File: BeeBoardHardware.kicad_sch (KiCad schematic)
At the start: 34 parts, among them J2 USB_C_Receptacle_USB2.0_16P, J3 Conn_01x02, Q1 Q_PMOS_DGS, Q2 2N3904, SW1 SW_Push, U1 MCP16311x-xMNY, U2 BQ24074RGT, U3 USBLC6-2SC6

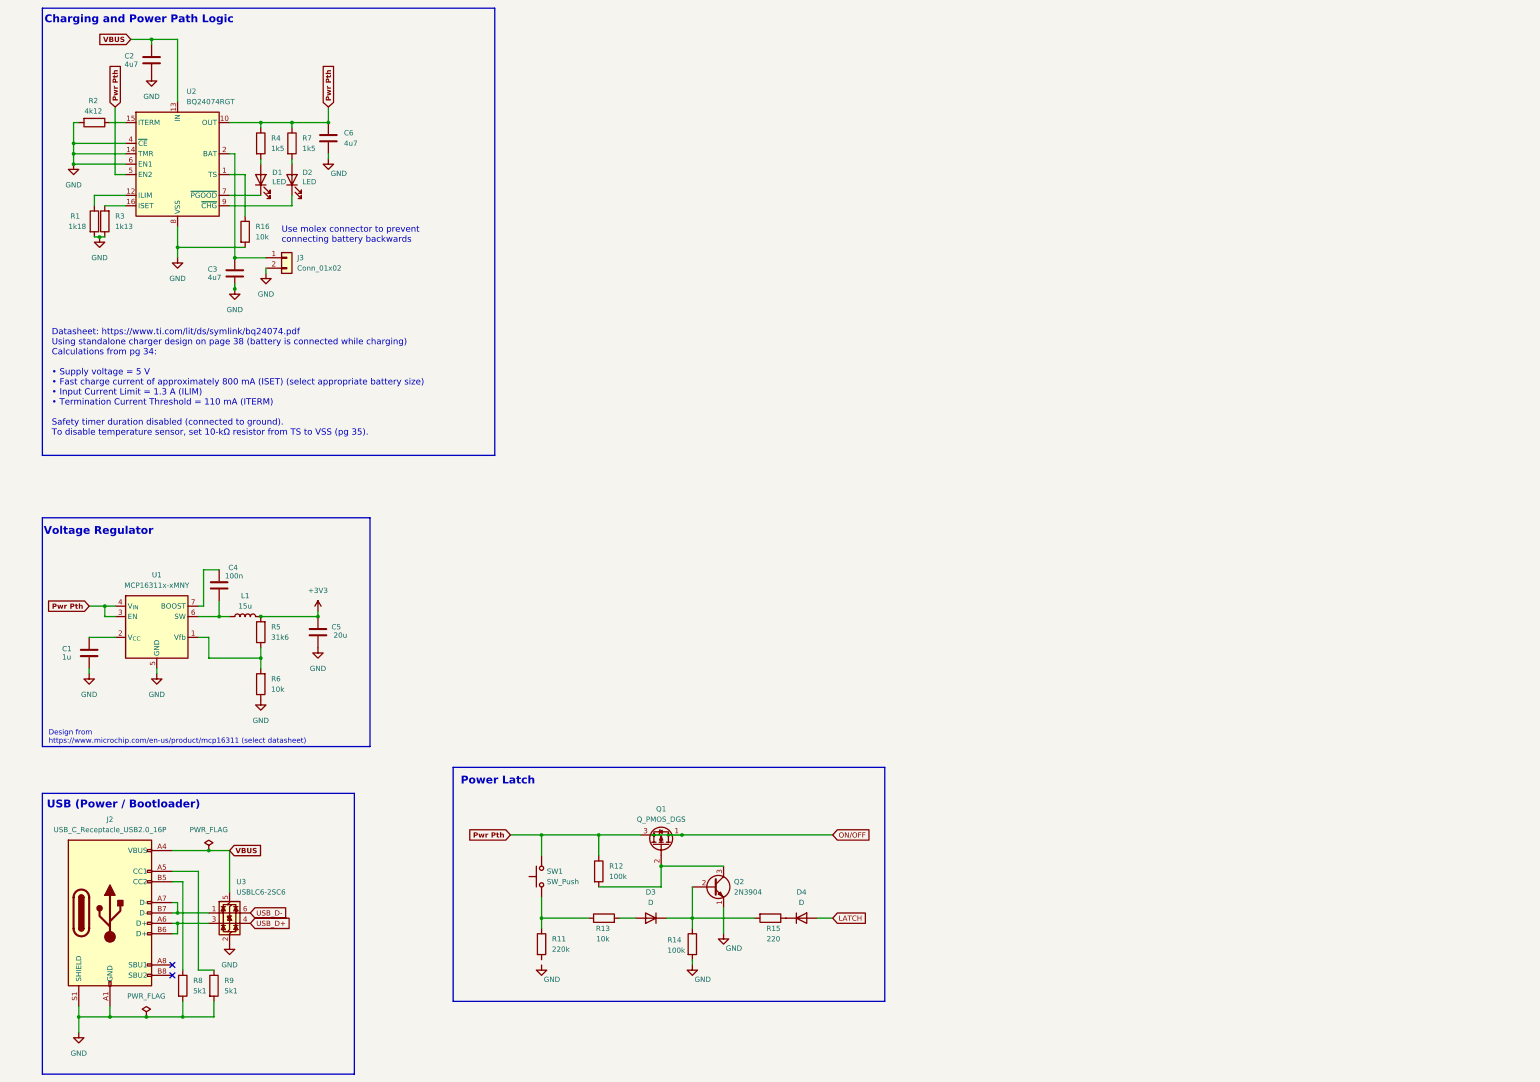
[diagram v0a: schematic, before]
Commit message: add readme and updated schematic
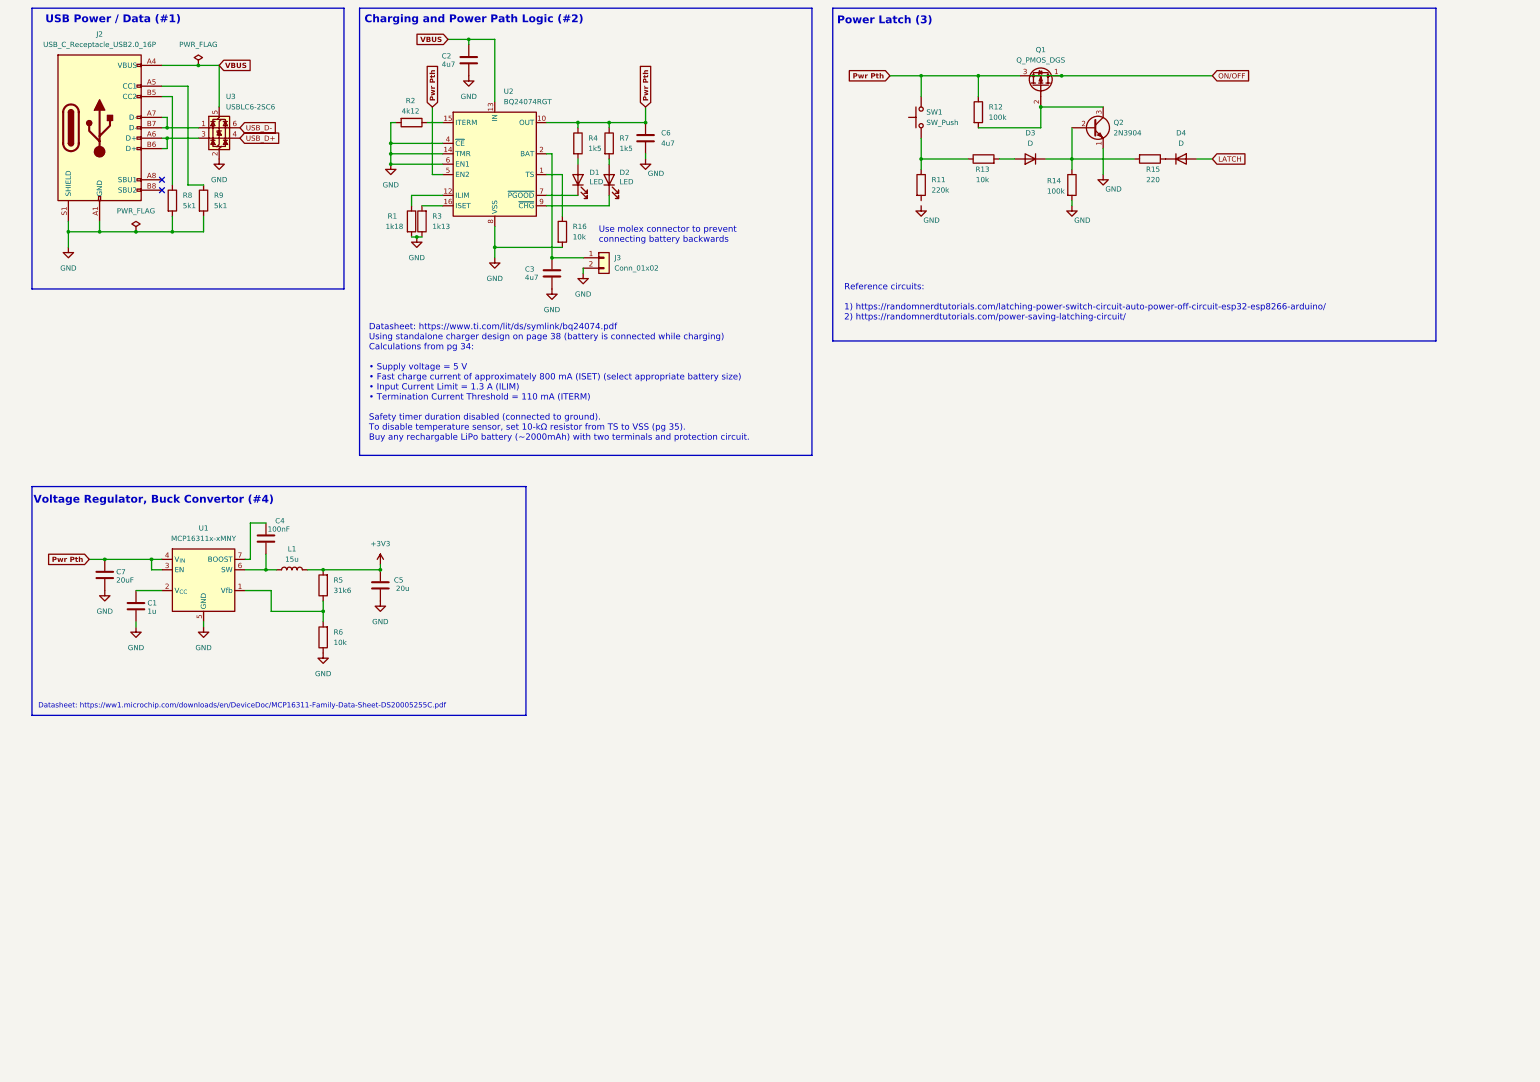
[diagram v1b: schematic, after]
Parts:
- added C7: 20uF, Capacitor_SMD:C_0402_1005Metric, symbol Device:C
- C4: value 100n -> 100nF
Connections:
- net GND: now also C7.2
- net Pwr Pth: now also C7.1
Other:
- note added: "Charging and Power Path Logic (#2)"
- note added: "Datasheet: https://ww1.microchip.com/downloads/en/DeviceDoc/MCP16311-Family-Data-Sheet-DS20005255C.pdf"
- note added: "Power Latch (3)"
- note added: "Reference circuits: 1) https://randomnerdtutorials.com/latching-power-switch-circuit-auto-power-off-circuit-esp32-esp8266-arduino/ 2) https://randomnerdtutorials.com/power-saving-latching-circuit/"
- note added: "USB Power / Data (#1)"
- note added: "Voltage Regulator, Buck Convertor (#4)"
- note removed: "Charging and Power Path Logic"
- note removed: "Design from https://www.microchip.com/en-us/product/mcp16311 (select datasheet)"
- note removed: "Power Latch"
- note removed: "USB (Power / Bootloader)"
- note removed: "Voltage Regulator"
- moved on the sheet: C1, C2, C3, C4, C5, C6, D1, D2, D3, D4, J2, J3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

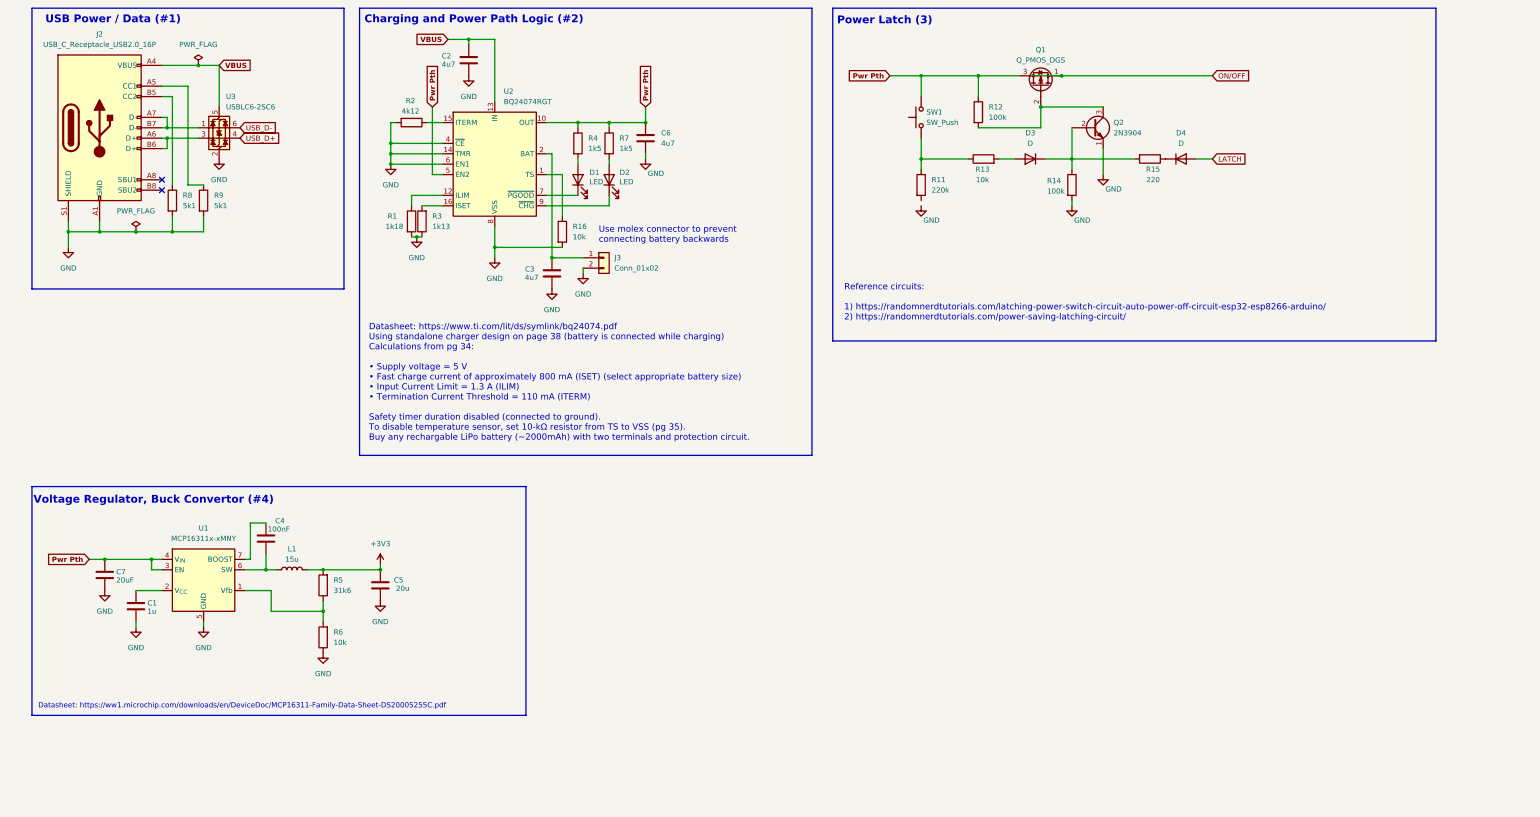
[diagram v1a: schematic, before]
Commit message: added battery monitor
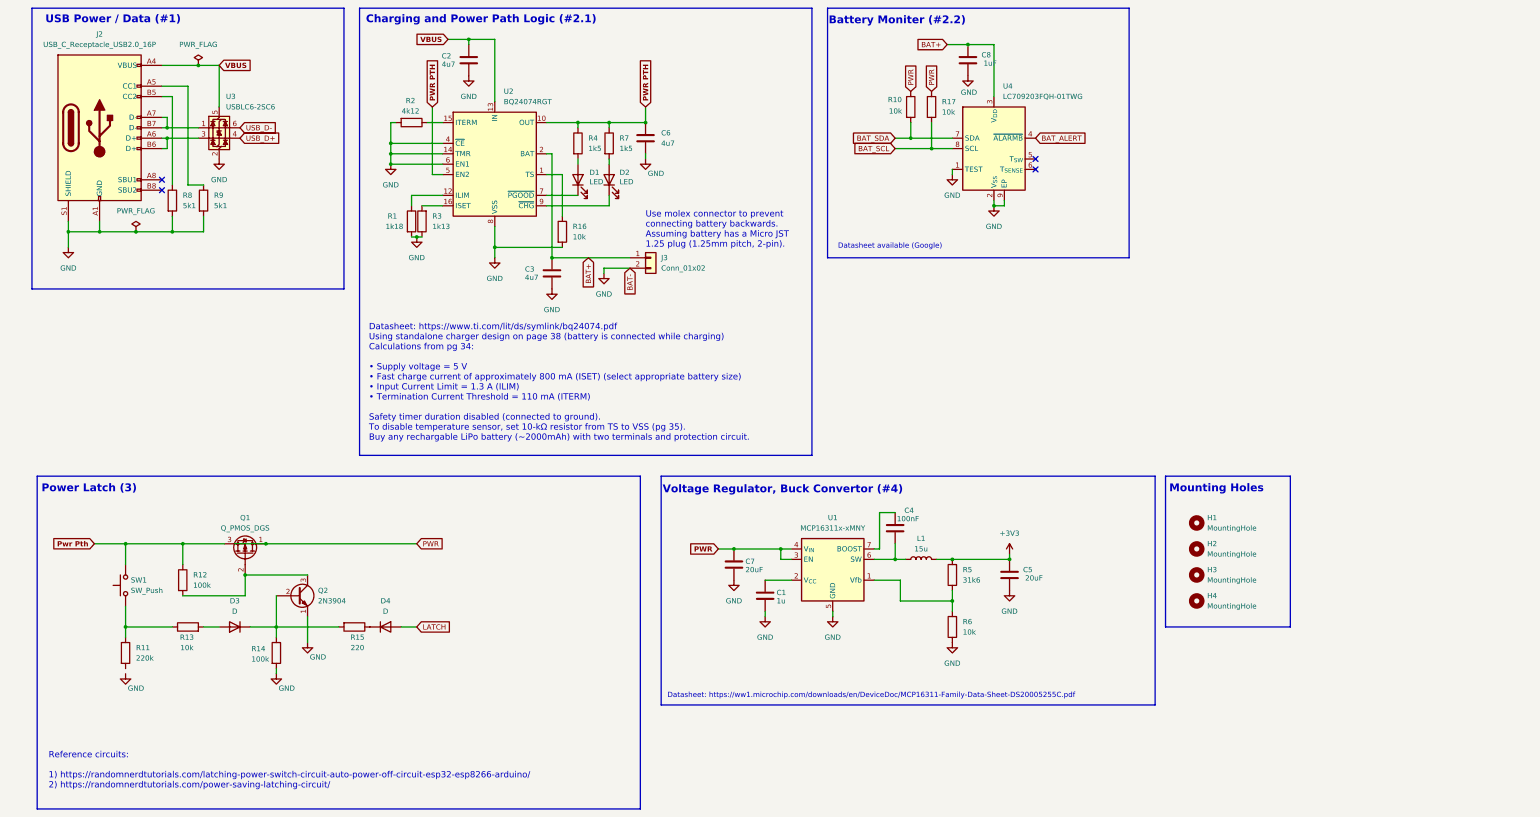
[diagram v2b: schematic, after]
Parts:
- added C8: 1uF, Capacitor_SMD:C_0402_1005Metric, symbol Device:C
- added H1, H2, H3, H4: MountingHole, symbol Mechanical:MountingHole
- added R10, R17: 10k, Resistor_SMD:R_0402_1005Metric, symbol Device:R
- added U4: LC709203FQH-01TWG, Package_DFN_QFN:WDFN-8-1EP_4x3mm_P0.65mm_EP2.4x1.8mm, symbol Battery_Management:LC709203FQH-01TWG
- C5: value 20u -> 20uF
- J2: Digikey Link (none) -> https://www.digikey.com/en/products/detail/gct/USB4520-03-0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; Manufacturer Product Number (none) -> USB4520-03-0-A
- J3: Digikey Link (none) -> https://www.digikey.com/en/products/detail/molex/0530470210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; Manufacturer Product Number (none) -> 0530470210
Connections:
- net GND: now also C8.2, U4.1 (TEST), U4.2 (V_{SS}), U4.9 (EP)
- net Pwr Pth: no longer C6.1, C7.1, R4.1, R7.1, U1.3 (EN), U1.4 (V_{IN}), U2.10 (OUT), U2.11 (OUT), U2.5 (EN2)
- net BAT+: now reaches C3.1, J3.1 (Pin_1), U2.2 (BAT), U2.3 (BAT)
- net BAT+: now also C8.1, U4.3 (V_{DD})
- net ON/OFF renamed PWR
- net PWR: now also C7.1, U1.3 (EN), U1.4 (V_{IN}), R10.1, R17.1
- new net BAT_ALERT: U4.4 (~{ALARMB})
- new net BAT_SCL: R17.2, U4.8 (SCL)
- new net BAT_SDA: R10.2, U4.7 (SDA)
- new net PWR PTH: C6.1, R4.1, R7.1, U2.10 (OUT), U2.11 (OUT), U2.5 (EN2)
- no-connect marks 2 -> 4
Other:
- note added: "Battery Moniter (#2.2)"
- note added: "Charging and Power Path Logic (#2.1)"
- note added: "Datasheet available (Google)"
- note added: "Mounting Holes"
- note added: "Use molex connector to prevent connecting battery backwards. Assuming battery has a Micro JST 1.25 plug (1.25mm pitch, 2-pin)."
- note removed: "Charging and Power Path Logic (#2)"
- note removed: "Use molex connector to prevent connecting battery backwards"
- moved on the sheet: C1, C4, C5, C7, D3, D4, J3, L1, Q1, Q2, R11, R12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

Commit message: updated schematic
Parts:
- removed Q2: 2N3904, Package_TO_SOT_THT:TO-92_Inline, symbol Transistor_BJT:2N3904
- added J1: Conn_01x10, symbol Connector_Generic:Conn_01x10
- added Q2, Q3: MMBT3904, Package_TO_SOT_SMD:SOT-23, symbol Transistor_BJT:MMBT3904
- added R18: 10k, Resistor_SMD:R_0402_1005Metric, symbol Device:R
- added R19: 1k, Resistor_SMD:R_0402_1005Metric, symbol Device:R
- added R20: 220k, Resistor_SMD:R_0402_1005Metric, symbol Device:R
- Q1: value Q_PMOS_DGS -> AO3413; Digikey Link (none) -> https://www.digikey.com/en/products/detail/alpha-omega-semi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; Manufacturer Product Number (none) -> AO3413
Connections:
- net BAT_ALERT: now also J1.2 (Pin_2)
- net BAT_SCL: now also J1.4 (Pin_4)
- net BAT_SDA: now also J1.3 (Pin_3)
- net GND: now also R11.2, J1.10 (Pin_10), Q3.2 (E), R20.2
- net LATCH: now also J1.8 (Pin_8)
- net Pwr Pth: now also R18.2
- net USB_D+: now also J1.6 (Pin_6)
- net USB_D-: now also J1.5 (Pin_5)
- net VBUS: now also J1.7 (Pin_7)
- net at R11.1, R13.1: now also Q2.2 (E); no longer SW1.1
- net at D3.1 (K), R14.1, R15.2: now also Q3.1 (B)
- net at Q1.2 (G), R12.2: now also Q3.3 (C)
- net +3V3 renamed +3v3
- net +3v3: now also J1.1 (Pin_1)
- new net: Q2.1 (B), R19.1
- new net: Q2.3 (C), R18.1
- new net TRIGGER: J1.9 (Pin_9), R19.2, R20.1, SW1.1
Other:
- note added: "Exlanations for headers: 1) +3v3: regulated output voltage 2) BAT_ALERT: interrupt from battery moniter 3) BAT_SDA: I2C for battery moniter 4) BAT_SCL: I2C for battery moniter 5) USB_D-: dataline 6) USB_D+: dataline 7) VBUS: USB bus 8) LATCH: GPIO to programtically turn off power 9) TRIGGER: power button to turn on/off power 10) GND: reference ground"
- note added: "Headers (#5)"
- moved on the sheet: C2, C3, C6, C8, D1, D2, D3, D4, J3, Q1, R1, R10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

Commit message: assign footprints
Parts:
- C4: value 100nF -> 100n
- C5, C7: value 20uF -> 20u
- C8: value 1uF -> 1u
- D3, D4: footprint (none) -> Diode_SMD:D_0402_1005Metric
- H1, H2, H3, H4: footprint (none) -> MountingHole:MountingHole_2.1mm
- J1: footprint (none) -> Connector_PinHeader_2.54mm:PinHeader_1x10_P2.54mm_Vertical
- J3: footprint (none) -> Connector_JST:JST_GH_BM02B-GHS-TBT_1x02-1MP_P1.25mm_Vertical
- Q1: footprint (none) -> Package_TO_SOT_SMD:SOT-23
- SW1: footprint (none) -> footprints:3983_switch; Digikey Link (none) -> https://www.digikey.com/en/products/detail/adafruit-industr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; Manufacturer Product Number (none) -> 3983
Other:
- note added: "Exlanations for headers: 1) +3v3: regulated output voltage 2) BAT_ALERT: interrupt from battery moniter 3) BAT_SDA: I2C for battery moniter 4) BAT_SCL: I2C for battery moniter 5) USB_D-: dataline 6) USB_D+: dataline 7) VBUS: USB bus 8) LATCH: GPIO to programtically turn off power 9) TRIGGER: manual power button to turn on/off power 10) GND: reference ground"
- note removed: "Exlanations for headers: 1) +3v3: regulated output voltage 2) BAT_ALERT: interrupt from battery moniter 3) BAT_SDA: I2C for battery moniter 4) BAT_SCL: I2C for battery moniter 5) USB_D-: dataline 6) USB_D+: dataline 7) VBUS: USB bus 8) LATCH: GPIO to programtically turn off power 9) TRIGGER: power button to turn on/off power 10) GND: reference ground"
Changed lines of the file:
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@@
 		)
 	)
-	(text "Exlanations for headers: \n1) +3v3: regulated output voltage\n2) BAT_ALERT: interrupt from battery moniter\n3) BAT_SDA: I2C for battery moniter\n4) BAT_SCL: I2C for battery moniter\n5) USB_D-: dataline\n6) USB_D+: dataline\n7) VBUS: USB bus\n8) LATCH: GPIO to programtically turn off power\n9) TRIGGER: power button to turn on/off power\n10) GND: reference ground"
+	(text "Exlanations for headers: \n1) +3v3: regulated output voltage\n2) BAT_ALERT: interrupt from battery moniter\n3) BAT_SDA: I2C for battery moniter\n4) BAT_SCL: I2C for battery moniter\n5) USB_D-: dataline\n6) USB_D+: dataline\n7) VBUS: USB bus\n8) LATCH: GPIO to programtically turn off power\n9) TRIGGER: manual power button to turn on/off power\n10) GND: reference ground"
 		(exclude_from_sim no)
 		(at 67.056 240.792 0)
@@
 			)
 		)
-		(property "Footprint" ""
+		(property "Footprint" "Diode_SMD:D_0402_1005Metric"
 			(at 118.11 180.34 0)
 			(effects
@@
 			)
 		)
-		(property "Footprint" ""
+		(property "Footprint" "footprints:3983_switch"
 			(at 146.05 167.64 0)
 			(effects
@@
 			)
 		)
+		(property "Digikey Link" "https://www.digikey.com/en/products/detail/adafruit-industries-llc/3983/9826291"
+			(at 151.13 167.64 0)
+			(effects
+				(font
+					(size 1.27 1.27)
+				)
+				(hide yes)
+			)
+		)
+		(property "Manufacturer Product Number" "3983"
+			(at 151.13 167.64 0)
+			(effects
+				(font
+					(size 1.27 1.27)
+				)
+				(hide yes)
+			)
+		)
 		(pin "1"
 		)
@@
 			)
 		)
-		(property "Footprint" ""
+		(property "Footprint" "Connector_PinHeader_2.54mm:PinHeader_1x10_P2.54mm_Vertical"
 			(at 46.99 241.3 0)
 			(effects
@@
 			)
 		)
-		(property "Value" "100nF"
+		(property "Value" "100n"
 			(at 238.252 143.764 0)
 			(effects
@@
 			)
 		)
-		(property "Value" "1uF"
+		(property "Value" "1u"
 			(at 246.38 32.512 0)
 			(effects
@@
 			)
 		)
-		(property "Footprint" ""
+		(property "Footprint" "MountingHole:MountingHole_2.1mm"
 			(at 306.07 163.83 0)
 			(effects
@@
 			)
 		)
-		(property "Footprint" ""
+		(property "Footprint" "MountingHole:MountingHole_2.1mm"
 			(at 306.07 157.48 0)
 			(effects
@@
 			)
 		)
-		(property "Footprint" ""
+		(property "Footprint" "Connector_JST:JST_GH_BM02B-GHS-TBT_1x02-1MP_P1.25mm_Vertical"
 			(at 165.1 80.01 0)
 			(effects
@@
 			)
 		)
-		(property "Value" "20uF"
+		(property "Value" "20u"
 			(at 264.16 158.242 0)
 			(effects
@@
 			)
 		)
-		(property "Footprint" ""
+		(property "Footprint" "Package_TO_SOT_SMD:SOT-23"
 			(at 86.36 146.05 0)
 			(effects
@@
 			)
 		)
-		(property "Footprint" ""
+		(property "Footprint" "Diode_SMD:D_0402_1005Metric"
 			(at 81.28 180.34 0)
 			(effects
@@
 			)
 		)
-		(property "Footprint" ""
+		(property "Footprint" "MountingHole:MountingHole_2.1mm"
 			(at 306.07 151.13 0)
 			(effects
@@
 			)
 		)
-		(property "Value" "20uF"
+		(property "Value" "20u"
 			(at 195.834 156.21 0)
 			(effects
@@
 			)
 		)
-		(property "Footprint" ""
+		(property "Footprint" "MountingHole:MountingHole_2.1mm"
 			(at 306.07 144.78 0)
 			(effects
